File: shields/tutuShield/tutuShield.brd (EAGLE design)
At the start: 22.8 x 22.9 mm, 20 parts, among them IC1 IC_MSGEQ7-SOIC8

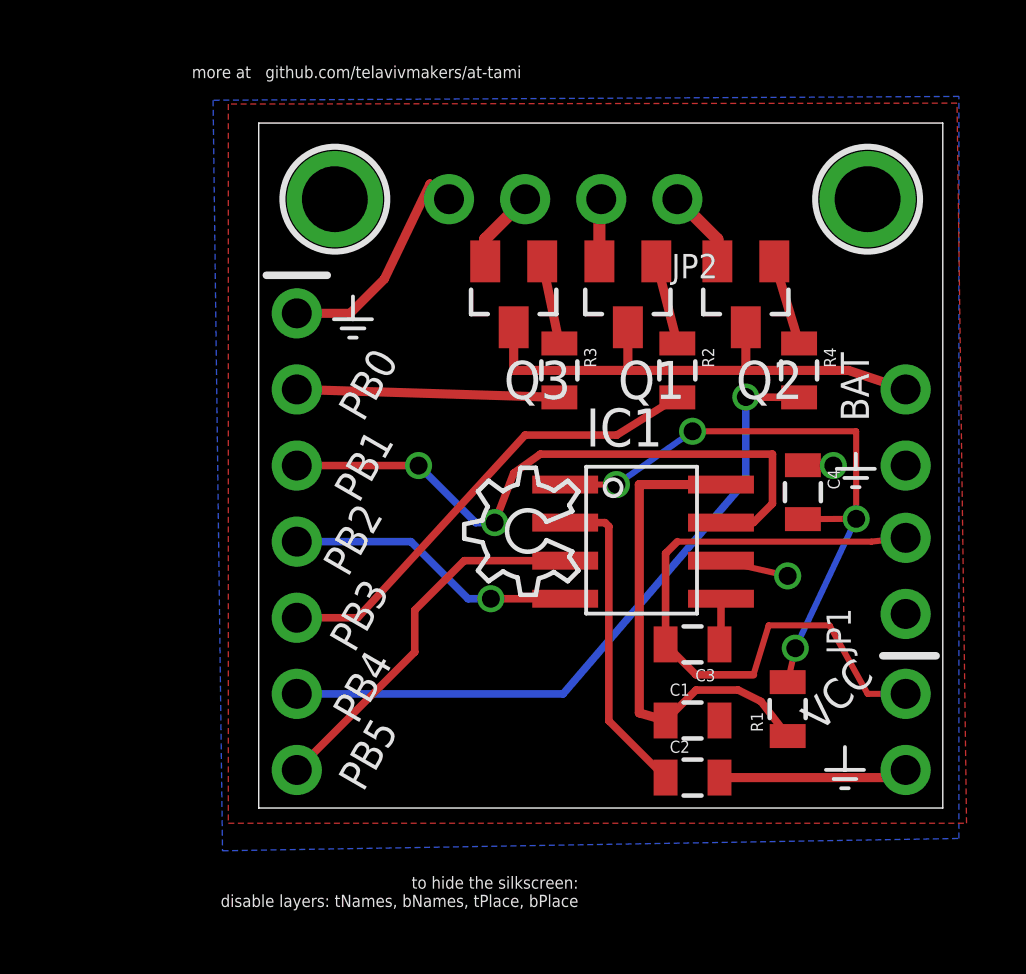
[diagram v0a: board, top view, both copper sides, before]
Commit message: added tutu logo and BMP file
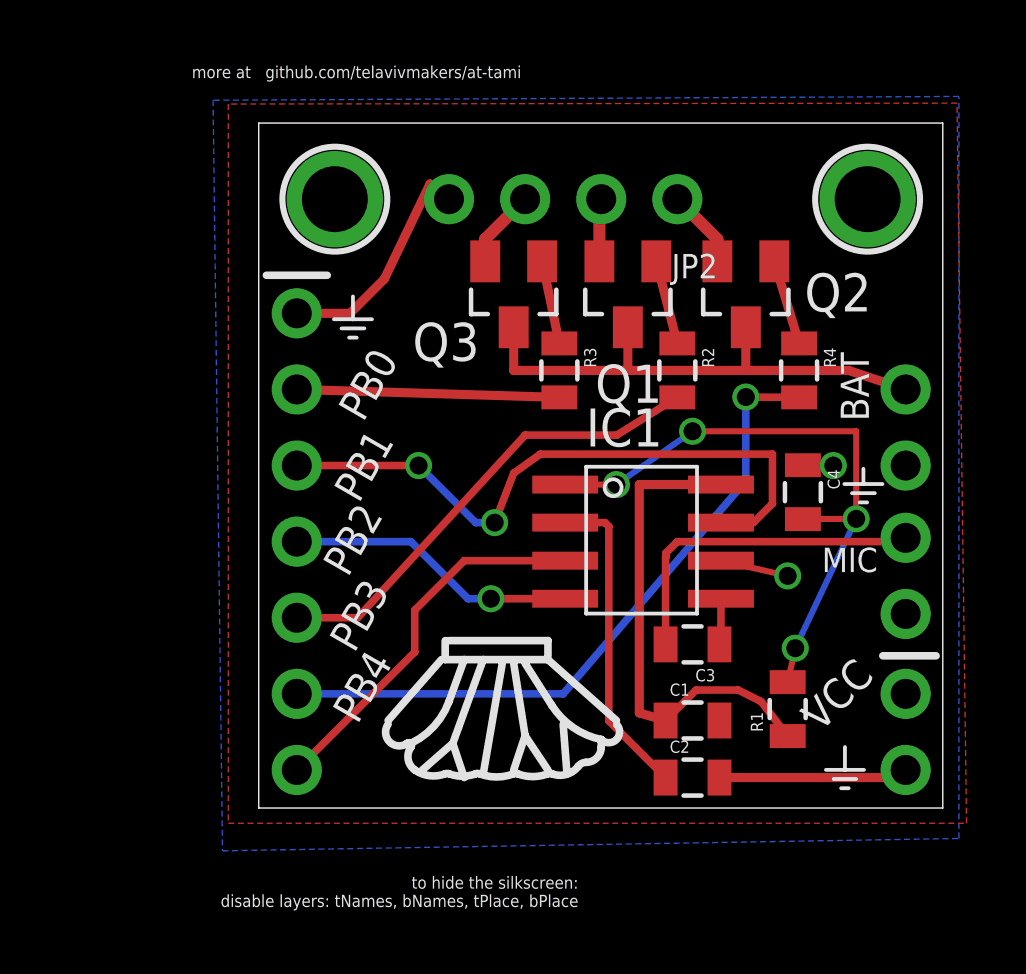
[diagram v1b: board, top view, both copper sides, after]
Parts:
- removed U$3: (no value), ohw-logo:OSHW_6X150_NOTEXT
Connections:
- new net N$1: C3.2, JP1.2
- net VCC: no longer C3.2, JP1.2
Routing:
- net VCC: track 22.2 -> 0.00 mm
- net N$1: track 0.00 -> 11.3 mm
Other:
- board text added: "MIC"

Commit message: fixed vcc wire bugs
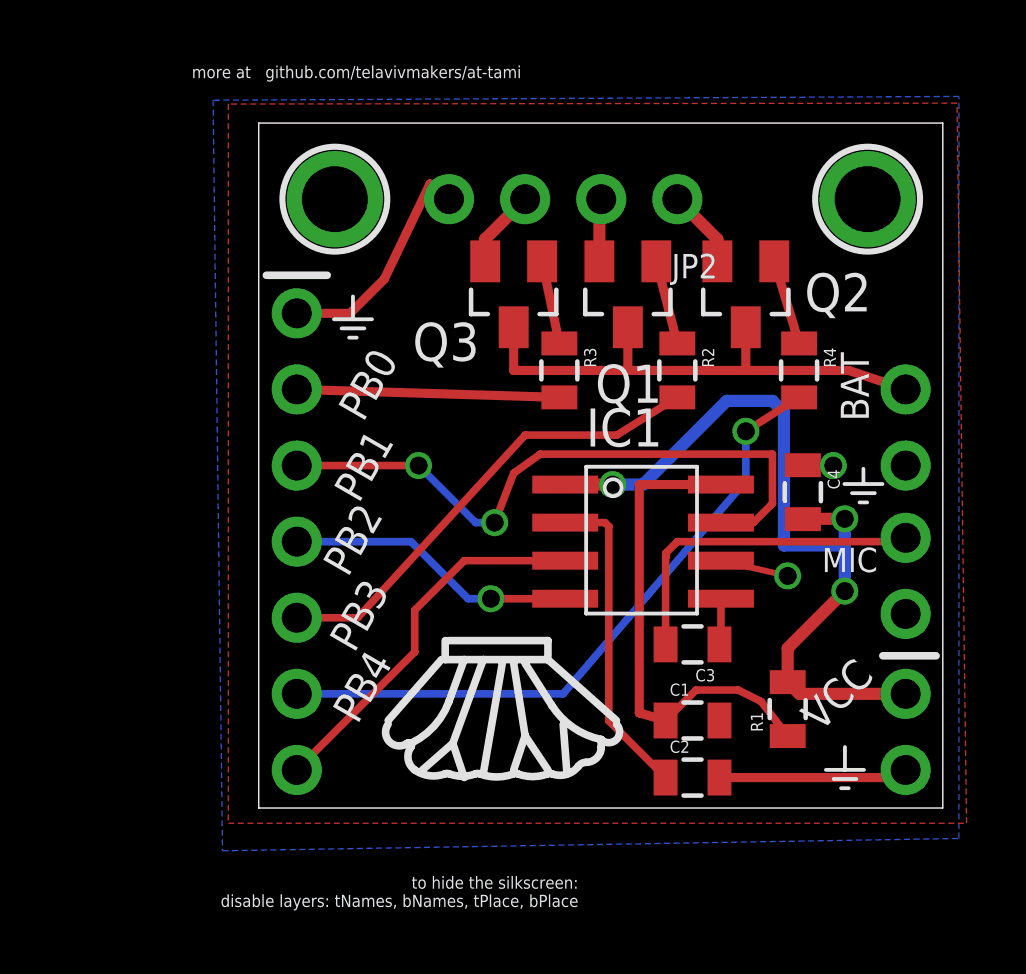
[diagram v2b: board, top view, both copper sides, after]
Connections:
- removed net VDDA: C4.2, IC1.1, R1.2
- net VCC: now also C4.2, IC1.1, R1.2
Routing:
- net VCC: track 0.00 -> 26.8 mm, vias 0 -> 3
- net VDDA: track 20.9 -> 0.00 mm, vias 4 -> 0
- net PB4: track 22.8 -> 22.0 mm
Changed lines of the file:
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@@
 <via x="19.177" y="11.43" extent="1-16" drill="0.6" shape="square"/>
-</signal>
-<signal name="VCC">
-<contactref element="J3" pad="1"/>
 </signal>
 <signal name="N$2">
@@
 <wire x1="1.27" y1="3.81" x2="10.16" y2="3.81" width="0.254" layer="16"/>
 <wire x1="10.16" y1="3.81" x2="16.256" y2="10.922" width="0.254" layer="16"/>
-<wire x1="16.256" y1="10.922" x2="16.256" y2="13.716" width="0.254" layer="16"/>
-<via x="16.256" y="13.716" extent="1-16" drill="0.6" shape="square"/>
-<wire x1="16.256" y1="13.716" x2="18.034" y2="13.705" width="0.254" layer="1"/>
+<wire x1="16.256" y1="10.922" x2="16.256" y2="12.573" width="0.254" layer="16"/>
+<via x="16.256" y="12.573" extent="1-16" drill="0.6" shape="square"/>
+<wire x1="16.256" y1="12.573" x2="18.034" y2="13.705" width="0.254" layer="1"/>
 </signal>
 <signal name="PB5">
@@
 <wire x1="7.559" y1="18.989" x2="8.89" y2="20.32" width="0.4064" layer="1"/>
 </signal>
-<signal name="VDDA">
-<contactref element="C4" pad="2"/>
-<contactref element="R1" pad="2"/>
-<contactref element="IC1" pad="1"/>
-<wire x1="17.653" y1="4.202" x2="17.907" y2="5.334" width="0.2032" layer="1"/>
-<via x="17.907" y="5.334" extent="1-16" drill="0.6" shape="square"/>
-<wire x1="17.907" y1="5.334" x2="19.939" y2="9.652" width="0.2032" layer="16"/>
-<via x="19.939" y="9.652" extent="1-16" drill="0.6" shape="square"/>
-<wire x1="19.939" y1="9.652" x2="18.161" y2="9.641" width="0.2032" layer="1"/>
-<wire x1="10.227" y1="10.795" x2="11.938" y2="10.795" width="0.2032" layer="1"/>
-<via x="11.938" y="10.795" extent="1-16" drill="0.6" shape="square"/>
-<wire x1="11.938" y1="10.795" x2="14.478" y2="12.573" width="0.2032" layer="16"/>
-<via x="14.478" y="12.573" extent="1-16" drill="0.6" shape="square"/>
-<wire x1="14.478" y1="12.573" x2="19.939" y2="12.573" width="0.2032" layer="1"/>
-<wire x1="19.939" y1="12.573" x2="19.939" y2="9.652" width="0.2032" layer="1"/>
-</signal>
 <signal name="N$1">
 <contactref element="C3" pad="2"/>
@@
 <wire x1="13.578" y1="8.371" x2="13.578" y2="5.461" width="0.254" layer="1"/>
 </signal>
+<signal name="VCC">
+<contactref element="IC1" pad="1"/>
+<contactref element="C4" pad="2"/>
+<contactref element="R1" pad="2"/>
+<contactref element="J3" pad="1"/>
+<wire x1="21.59" y1="3.81" x2="18.045" y2="3.81" width="0.4064" layer="1"/>
+<wire x1="18.045" y1="3.81" x2="17.653" y2="4.202" width="0.4064" layer="1"/>
+<wire x1="17.653" y1="4.202" x2="17.653" y2="5.334" width="0.4064" layer="1"/>
+<wire x1="17.653" y1="5.334" x2="19.558" y2="7.239" width="0.4064" layer="1"/>
+<via x="19.558" y="7.239" extent="1-16" drill="0.6" shape="square"/>
+<wire x1="19.558" y1="7.239" x2="19.558" y2="8.763" width="0.4064" layer="16"/>
+<via x="19.558" y="9.652" extent="1-16" drill="0.6" shape="square"/>
+<wire x1="19.558" y1="8.763" x2="19.558" y2="9.652" width="0.4064" layer="16"/>
+<wire x1="19.558" y1="9.652" x2="18.172" y2="9.652" width="0.4064" layer="1"/>
+<wire x1="18.172" y1="9.652" x2="18.161" y2="9.641" width="0.4064" layer="1"/>
+<wire x1="10.227" y1="10.795" x2="11.811" y2="10.795" width="0.4064" layer="1"/>
+<via x="11.811" y="10.795" extent="1-16" drill="0.6" shape="square"/>
+<wire x1="11.811" y1="10.795" x2="12.827" y2="10.795" width="0.4064" layer="16"/>
+<wire x1="12.827" y1="10.795" x2="15.621" y2="13.589" width="0.4064" layer="16"/>
+<wire x1="15.621" y1="13.589" x2="17.145" y2="13.589" width="0.4064" layer="16"/>
+<wire x1="17.145" y1="13.589" x2="17.526" y2="13.208" width="0.4064" layer="16"/>
+<wire x1="17.526" y1="13.208" x2="17.526" y2="8.763" width="0.4064" layer="16"/>
+<wire x1="17.526" y1="8.763" x2="19.558" y2="8.763" width="0.4064" layer="16"/>
+</signal>
 </signals>

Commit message: added tutu images and caption
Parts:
- moved C4 3.31 mm to (17.9, 7.24)
- moved R1 0.63 mm to (17.1, 3.68)
- moved C1 0.13 mm to (14.6, 2.92), turned to 180 degrees
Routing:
- net GND: track 17.6 -> 8.85 mm, vias 2 -> 0
- net CKIN: track 16.4 -> 14.0 mm
- net VCC: track 26.8 -> 24.8 mm, vias 3 -> 2
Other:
- board text added: "B"
- board text added: "G"
- board text added: "Midburn 2015 Tutu Shield"
- board text added: "R"
- board text added: "by Maayan Dreamer"
- board text removed: "+"
- board text removed: "V 0.00"

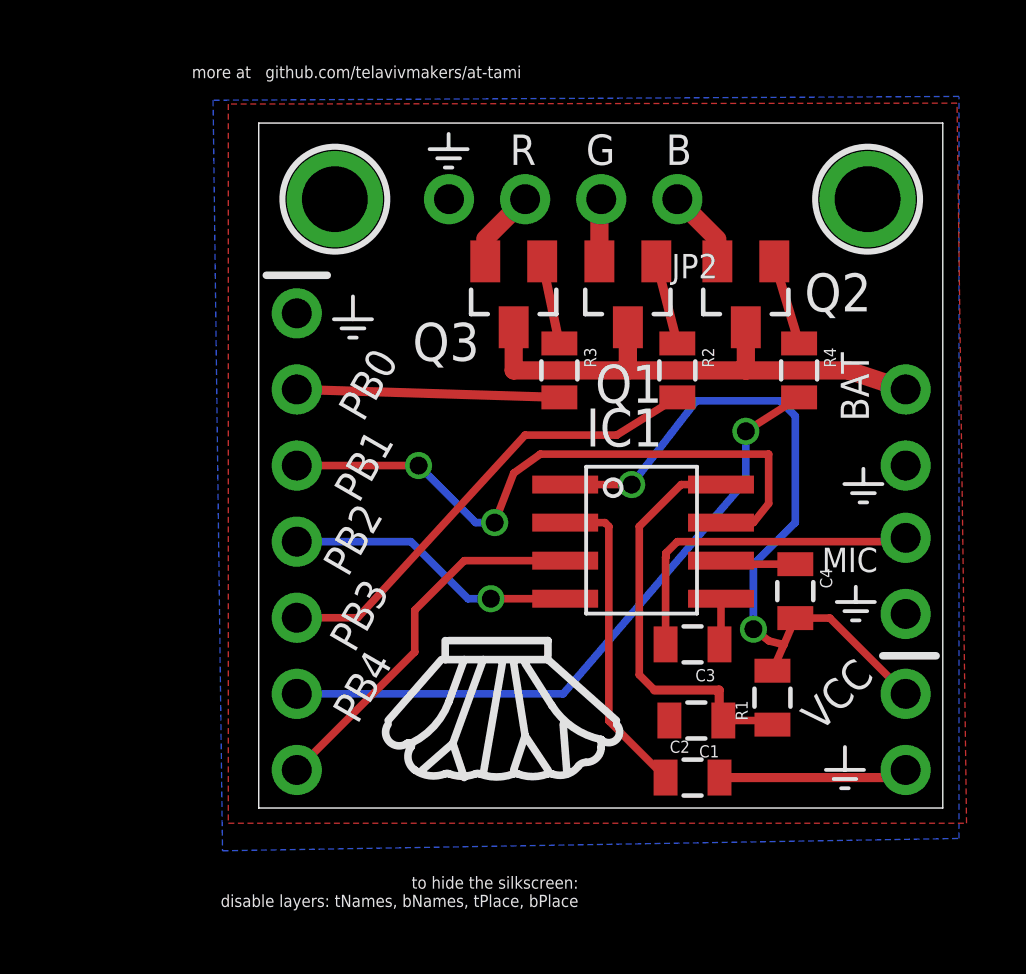
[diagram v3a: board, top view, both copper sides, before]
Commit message: fixed sizes of silkscreen fonts (was smaller then 32mil)
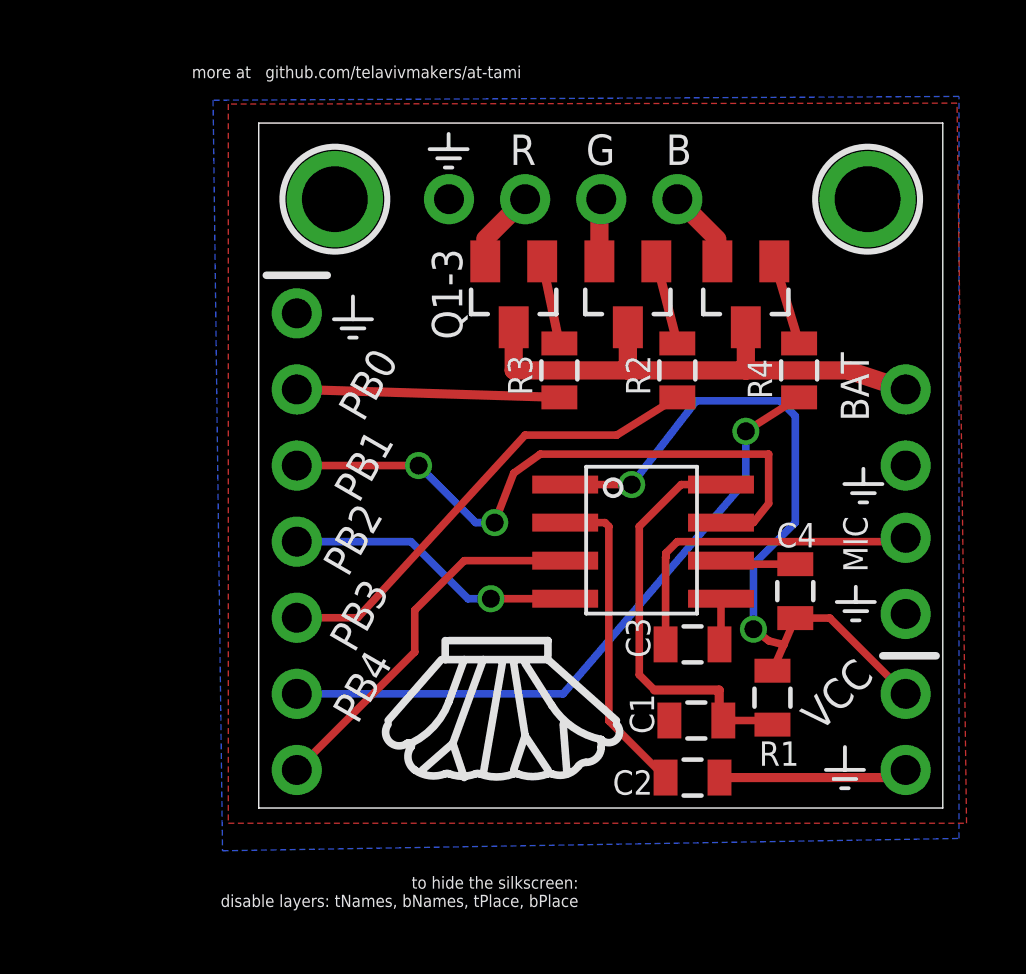
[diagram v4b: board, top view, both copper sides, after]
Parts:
- renumbered Q3 to Q1-3

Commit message: rewire the npn transistors
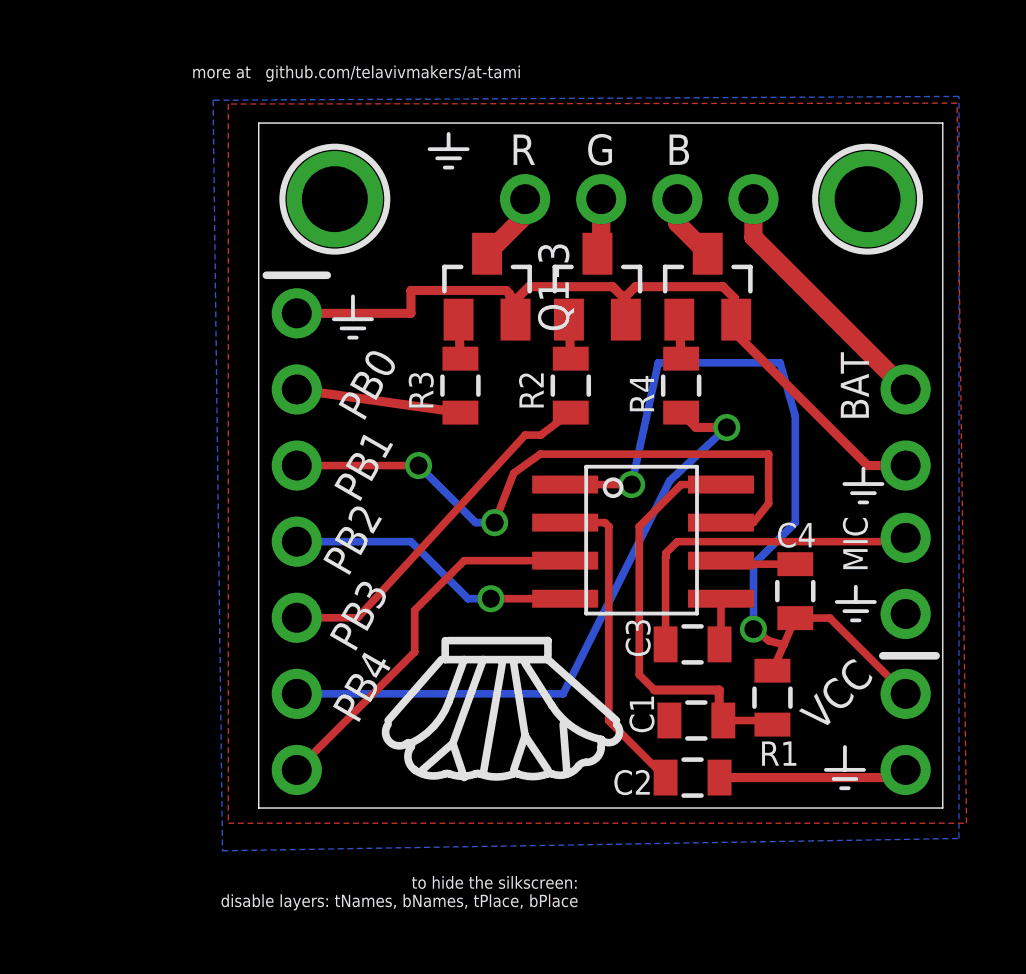
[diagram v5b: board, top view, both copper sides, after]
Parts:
- moved R4 3.97 mm to (14.1, 14.1)
- moved R2 3.59 mm to (10.4, 14.1)
- moved R3 3.34 mm to (6.73, 14.1)
- moved JP2 2.54 mm to (12.7, 20.3)
- moved Q2 1.30 mm to (15.0, 17.4), turned to 0 degrees
- moved Q1 1.05 mm to (11.3, 17.4), turned to 0 degrees
- moved Q1-3 0.92 mm to (7.62, 17.4), turned to 0 degrees
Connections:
- removed net N$10: JP2.1, Q2.2
- removed net N$11: JP2.2, Q1.2
- removed net N$13: JP2.3, Q1-3.2
- new net N$14: JP2.3, Q1.3
- new net N$4: JP2.2, Q2.3
- new net N$8: JP2.4, Q1-3.3
- net GND: now also Q1-3.2, Q1.2, Q2.2; no longer JP2.4
- net V_BAT: now also JP2.1; no longer Q1-3.3, Q1.3, Q2.3
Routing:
- net GND: track 8.85 -> 36.4 mm
- net V_BAT: track 17.5 -> 8.45 mm
- net PB3: track 15.7 -> 12.1 mm
- net PB0: track 8.77 -> 5.52 mm
- net VCC: track 24.8 -> 27.8 mm
- net N$10: track 2.63 -> 0.00 mm
- net N$13: track 2.63 -> 0.00 mm
- net N$8: track 0.00 -> 2.35 mm
- net N$4: track 0.00 -> 2.24 mm
- net N$11: track 2.10 -> 0.00 mm
- net N$14: track 0.00 -> 1.87 mm
- net N$7: track 2.86 -> 1.30 mm
- net N$6: track 2.83 -> 1.30 mm
- net N$3: track 2.80 -> 1.30 mm
- net PB4: track 22.0 -> 21.2 mm

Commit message: fixed pwm misshap in tutu shield
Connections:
- net PB1: now also R2.2; no longer IC1.7
- net PB3: now also IC1.7; no longer R2.2
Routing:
- net PB3: track 12.1 -> 10.8 mm
- net PB1: track 21.4 -> 20.3 mm
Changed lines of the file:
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@@
 <layer number="20" name="Dimension" color="15" fill="1" visible="yes" active="yes"/>
 <layer number="21" name="tPlace" color="16" fill="1" visible="yes" active="yes"/>
-<layer number="22" name="bPlace" color="14" fill="1" visible="no" active="yes"/>
+<layer number="22" name="bPlace" color="14" fill="1" visible="yes" active="yes"/>
 <layer number="23" name="tOrigins" color="15" fill="1" visible="yes" active="yes"/>
-<layer number="24" name="bOrigins" color="15" fill="1" visible="no" active="yes"/>
+<layer number="24" name="bOrigins" color="15" fill="1" visible="yes" active="yes"/>
 <layer number="25" name="tNames" color="7" fill="1" visible="no" active="yes"/>
 <layer number="26" name="bNames" color="7" fill="1" visible="no" active="yes"/>
@@
 <signal name="PB1">
 <contactref element="J1" pad="3"/>
-<contactref element="IC1" pad="7"/>
-<wire x1="15.427" y1="9.525" x2="16.51" y2="9.525" width="0.254" layer="1"/>
 <wire x1="16.51" y1="9.525" x2="17.018" y2="10.16" width="0.254" layer="1"/>
 <wire x1="17.018" y1="10.16" x2="17.018" y2="11.811" width="0.254" layer="1"/>
@@
 <via x="5.334" y="11.43" extent="1-16" drill="0.6" shape="square"/>
 <wire x1="5.334" y1="11.43" x2="1.27" y2="11.43" width="0.254" layer="1"/>
+<contactref element="R2" pad="2"/>
+<wire x1="9.398" y1="11.811" x2="10.414" y2="13.197" width="0" layer="19" extent="1-1"/>
 </signal>
 <signal name="PB2">
@@
 <signal name="PB3">
 <contactref element="J1" pad="5"/>
-<contactref element="R2" pad="2"/>
 <wire x1="1.27" y1="6.35" x2="3.302" y2="6.35" width="0.254" layer="1"/>
 <wire x1="3.302" y1="6.35" x2="8.89" y2="12.446" width="0.254" layer="1"/>
 <wire x1="8.89" y1="12.446" x2="9.409" y2="12.446" width="0.254" layer="1"/>
-<wire x1="9.409" y1="12.446" x2="10.414" y2="13.197" width="0.254" layer="1"/>
+<contactref element="IC1" pad="7"/>
+<wire x1="9.409" y1="12.446" x2="15.427" y2="9.525" width="0" layer="19" extent="1-1"/>
 </signal>
 <signal name="PB4">
